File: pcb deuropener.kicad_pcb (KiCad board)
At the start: 2 copper layers, 54.6 x 86.4 mm, 34 parts, among them J1 LED 1, J10 Duo LED, J11 Barrel_Jack_Switch, J12 RFID RC522, J13 Solenoid 12V, J14 jumper, J2 Button 2, J3 LED 2, J4 Button 1, J5 Buzzer 12V, P8 BeagleBone_Black_Header, P9 BeagleBone_Black_Header, Q1 STU60N3LH5, Q2 STU60N3LH5, U1 TSR_1-2450

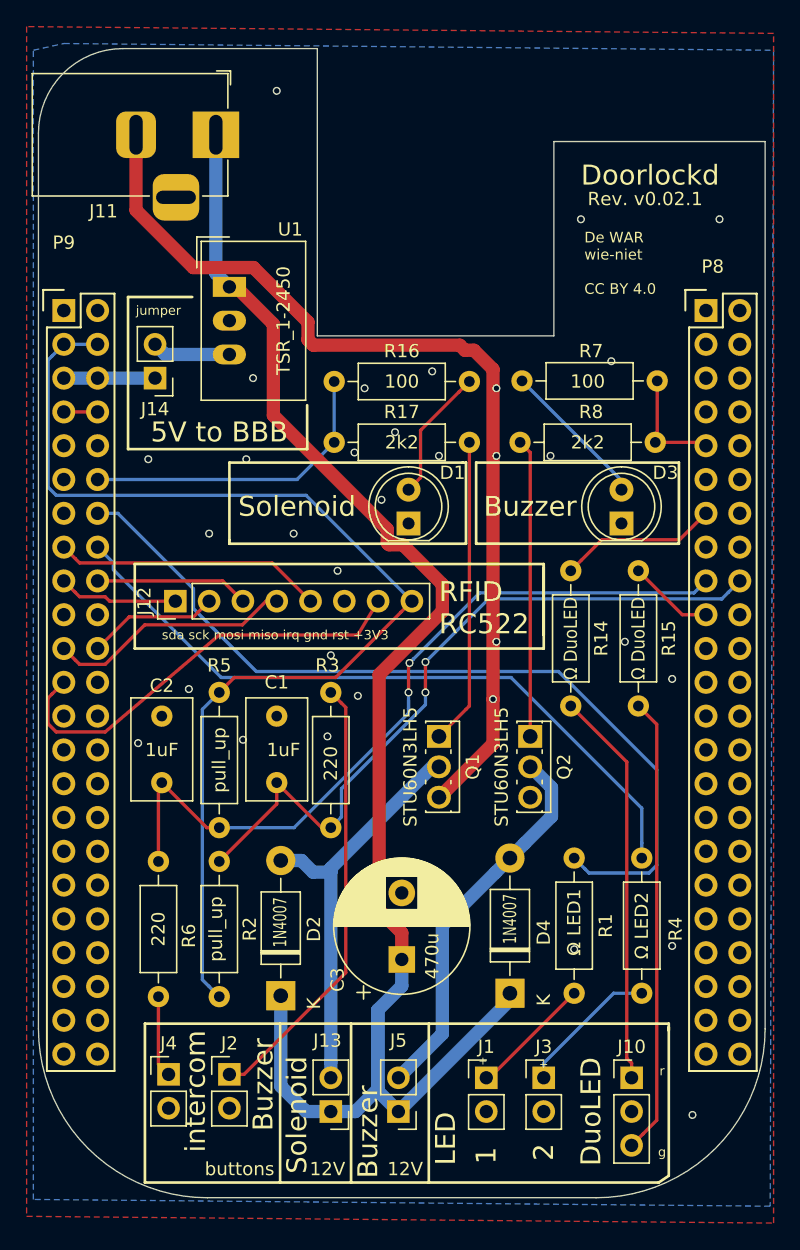
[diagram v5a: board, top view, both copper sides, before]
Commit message: Remove a lot of parts and traces
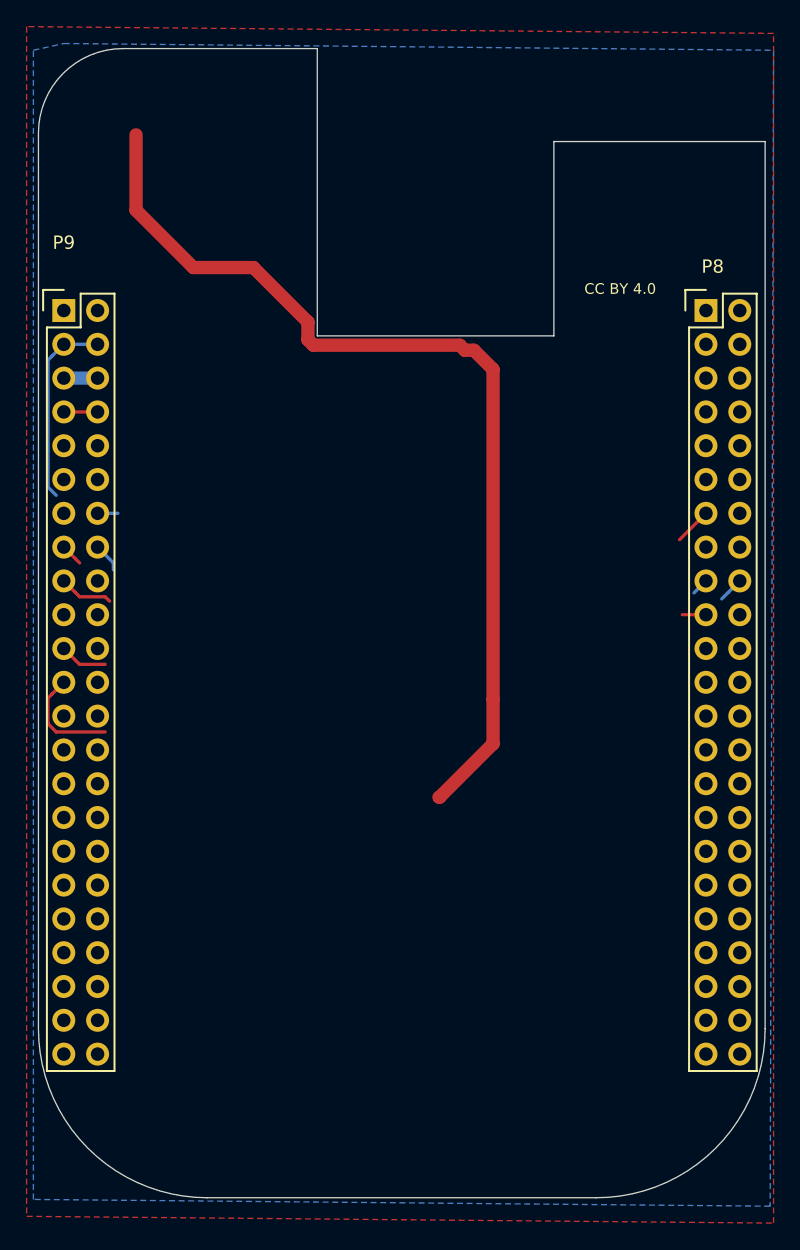
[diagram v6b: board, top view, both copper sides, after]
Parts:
- removed C1, C2: 1uF, Capacitor_THT:C_Disc_D7.5mm_W4.4mm_P5.00mm
- removed C3: 470u, Capacitor_THT:CP_Radial_D10.0mm_P5.00mm
- removed D1, D3: LED, LED_THT:LED_D5.0mm
- removed D2, D4: 1N4007, Diode_THT:D_DO-41_SOD81_P10.16mm_Horizontal
- removed J1: LED 1, Connector_PinHeader_2.54mm:PinHeader_1x02_P2.54mm_Vertical
- removed J10: Duo LED, Connector_PinHeader_2.54mm:PinHeader_1x03_P2.54mm_Vertical
- removed J11: Barrel_Jack_Switch, Connector_BarrelJack:BarrelJack_Horizontal
- removed J12: RFID RC522, Connector_PinHeader_2.54mm:PinHeader_1x08_P2.54mm_Vertical
- removed J13: Solenoid 12V, Connector_PinHeader_2.54mm:PinHeader_1x02_P2.54mm_Vertical
- removed J14: jumper, Connector_PinHeader_2.54mm:PinHeader_1x02_P2.54mm_Vertical
- removed J2: Button 2, Connector_PinHeader_2.54mm:PinHeader_1x02_P2.54mm_Vertical
- removed J3: LED 2, Connector_PinHeader_2.54mm:PinHeader_1x02_P2.54mm_Vertical
- removed J4: Button 1, Connector_PinHeader_2.54mm:PinHeader_1x02_P2.54mm_Vertical
- removed J5: Buzzer 12V, Connector_PinHeader_2.54mm:PinHeader_1x02_P2.54mm_Vertical
- removed Q1, Q2: STU60N3LH5, Package_TO_SOT_THT:SIPAK_Vertical
- removed R1: Ω LED1, Resistor_THT:R_Axial_DIN0207_L6.3mm_D2.5mm_P10.16mm_Horizontal
- removed R14, R15: Ω DuoLED, Resistor_THT:R_Axial_DIN0207_L6.3mm_D2.5mm_P10.16mm_Horizontal
- removed R16, R7: 100, Resistor_THT:R_Axial_DIN0207_L6.3mm_D2.5mm_P10.16mm_Horizontal
- removed R17, R8: 2k2, Resistor_THT:R_Axial_DIN0207_L6.3mm_D2.5mm_P10.16mm_Horizontal
- removed R2, R5: pull_up, Resistor_THT:R_Axial_DIN0207_L6.3mm_D2.5mm_P10.16mm_Horizontal
- removed R3, R6: 220, Resistor_THT:R_Axial_DIN0207_L6.3mm_D2.5mm_P10.16mm_Horizontal
- removed R4: Ω LED2, Resistor_THT:R_Axial_DIN0207_L6.3mm_D2.5mm_P10.16mm_Horizontal
- removed U1: TSR_1-2450, Converter_DCDC:Converter_DCDC_TRACO_TSR-1_THT
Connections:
- P8 pad 10: (no net) -> Net-(P8-Pad10)
- P8 pad 11: (no net) -> Net-(P8-Pad11)
- P8 pad 12: (no net) -> Net-(P8-Pad12)
- P8 pad 13: IO-P8_13-UI_DuoLED1r -> Net-(P8-Pad13)
- P8 pad 14: (no net) -> Net-(P8-Pad14)
- P8 pad 15: (no net) -> Net-(P8-Pad15)
- P8 pad 16: (no net) -> Net-(P8-Pad16)
- P8 pad 17: IO-P8_17-Button1 -> Net-(P8-Pad17)
- P8 pad 18: IO-P8_18-Button2 -> Net-(P8-Pad18)
- P8 pad 19: IO-P8_19-UI_DuoLED1g -> Net-(P8-Pad19)
- P8 pad 20: (no net) -> Net-(P8-Pad20)
- P8 pad 21: (no net) -> Net-(P8-Pad21)
- P8 pad 22: (no net) -> Net-(P8-Pad22)
- P8 pad 23: (no net) -> Net-(P8-Pad23)
- P8 pad 24: (no net) -> Net-(P8-Pad24)
- P8 pad 25: (no net) -> Net-(P8-Pad25)
- P8 pad 26: (no net) -> Net-(P8-Pad26)
- P8 pad 27: (no net) -> Net-(P8-Pad27)
- P8 pad 28: (no net) -> Net-(P8-Pad28)
- P8 pad 29: (no net) -> Net-(P8-Pad29)
- P8 pad 3: (no net) -> Net-(P8-Pad3)
- P8 pad 30: (no net) -> Net-(P8-Pad30)
- P8 pad 31: (no net) -> Net-(P8-Pad31)
- P8 pad 32: (no net) -> Net-(P8-Pad32)
- P8 pad 33: (no net) -> Net-(P8-Pad33)
- P8 pad 34: (no net) -> Net-(P8-Pad34)
- P8 pad 35: (no net) -> Net-(P8-Pad35)
- P8 pad 36: (no net) -> Net-(P8-Pad36)
- P8 pad 37: (no net) -> Net-(P8-Pad37)
- P8 pad 38: (no net) -> Net-(P8-Pad38)
- P8 pad 39: (no net) -> Net-(P8-Pad39)
- P8 pad 4: (no net) -> Net-(P8-Pad4)
- P8 pad 40: (no net) -> Net-(P8-Pad40)
- P8 pad 41: (no net) -> Net-(P8-Pad41)
- P8 pad 42: (no net) -> Net-(P8-Pad42)
- P8 pad 43: (no net) -> Net-(P8-Pad43)
- P8 pad 44: (no net) -> Net-(P8-Pad44)
- P8 pad 45: (no net) -> Net-(P8-Pad45)
- P8 pad 46: (no net) -> Net-(P8-Pad46)
- P8 pad 5: (no net) -> Net-(P8-Pad5)
- P8 pad 6: (no net) -> Net-(P8-Pad6)
- P8 pad 7: (no net) -> Net-(P8-Pad7)
- P8 pad 8: (no net) -> Net-(P8-Pad8)
- P8 pad 9: IO-P8_09-Buzzer -> Net-(P8-Pad9)
- P9 pad 10: (no net) -> Net-(P9-Pad10)
- P9 pad 11: (no net) -> Net-(P9-Pad11)
- P9 pad 12: IO-P9_12-Solenoid -> Net-(P9-Pad12)
- P9 pad 13: (no net) -> Net-(P9-Pad13)
- P9 pad 14: IO-P9_14-UILED1 -> Net-(P9-Pad14)
- P9 pad 15: IO-P9_15-RC522_IRQ -> Net-(P9-Pad15)
- P9 pad 16: IO-P9_16-UILED2 -> Net-(P9-Pad16)
- P9 pad 17: IO-P9_17-RC522_SDA -> Net-(P9-Pad17)
- P9 pad 18: IO-P9_18-RC522_MOSI -> Net-(P9-Pad18)
- P9 pad 19: (no net) -> Net-(P9-Pad19)
- P9 pad 20: (no net) -> Net-(P9-Pad20)
- P9 pad 21: IO-P9_21-RC522_MISO -> Net-(P9-Pad21)
- P9 pad 22: IO-P9_22-RC522_SCK -> Net-(P9-Pad22)
- P9 pad 23: IO-P9_23-RC522_RST -> Net-(P9-Pad23)
- P9 pad 24: (no net) -> Net-(P9-Pad24)
- P9 pad 25: (no net) -> Net-(P9-Pad25)
- P9 pad 26: (no net) -> Net-(P9-Pad26)
- P9 pad 27: (no net) -> Net-(P9-Pad27)
- P9 pad 28: (no net) -> Net-(P9-Pad28)
- P9 pad 29: (no net) -> Net-(P9-Pad29)
- P9 pad 30: (no net) -> Net-(P9-Pad30)
- P9 pad 31: (no net) -> Net-(P9-Pad31)
- P9 pad 32: (no net) -> VDD_ADC
- P9 pad 33: (no net) -> Net-(P9-Pad33)
- P9 pad 34: (no net) -> GNDA_ADC
- P9 pad 35: (no net) -> Net-(P9-Pad35)
- P9 pad 36: (no net) -> Net-(P9-Pad36)
- P9 pad 37: (no net) -> Net-(P9-Pad37)
- P9 pad 38: (no net) -> Net-(P9-Pad38)
- P9 pad 39: (no net) -> Net-(P9-Pad39)
- P9 pad 40: (no net) -> Net-(P9-Pad40)
- P9 pad 41: (no net) -> Net-(P9-Pad41)
- P9 pad 42: (no net) -> Net-(P9-Pad42)
- P9 pad 9: (no net) -> Net-(P9-Pad9)
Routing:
- net +12V: track 119.3 -> 0.00 mm
- net +3V3: track 85.9 -> 14.6 mm
- net IO-P9_14-UILED1: track 65.0 -> 0.00 mm
- net IO-P8_17-Button1: track 58.8 -> 0.00 mm, vias 2 -> 0
- net IO-P8_18-Button2: track 54.7 -> 0.00 mm, vias 2 -> 0
- net IO-P9_16-UILED2: track 53.1 -> 0.00 mm
- net Net-(J10-Pad3): track 34.4 -> 0.00 mm
- net Net-(J2-Pad1): track 33.4 -> 0.00 mm
- net IO-P9_23-RC522_RST: track 32.8 -> 0.00 mm
- net Net-(D2-Pad2): track 31.3 -> 0.00 mm
- net Net-(J10-Pad1): track 29.8 -> 0.00 mm
- net Net-(D4-Pad2): track 28.8 -> 0.00 mm
- net IO-P9_12-Solenoid: track 23.5 -> 0.00 mm
- net Net-(Q1-Pad1): track 23.0 -> 0.00 mm
- net Net-(Q2-Pad1): track 22.4 -> 0.00 mm
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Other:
- board text added: "CC BY 4.0"
- board text removed: "+"
- board text removed: "1"
- board text removed: "12V"
- board text removed: "2"
- board text removed: "5V to BBB"
- board text removed: "Buzzer"
- board text removed: "De WAR wie-niet CC BY 4.0"
- board text removed: "Doorlockd"
- board text removed: "DuoLED"
- board text removed: "LED"
- board text removed: "RFID RC522"
- board text removed: "Rev. v0.02.1"
- board text removed: "Solenoid"
- board text removed: "buttons"
- board text removed: "g"
- board text removed: "intercom"
- board text removed: "jumper"
- board text removed: "r"
- board text removed: "sda sck mosi miso irq gnd rst +3V3"

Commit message: convert to kicad 6
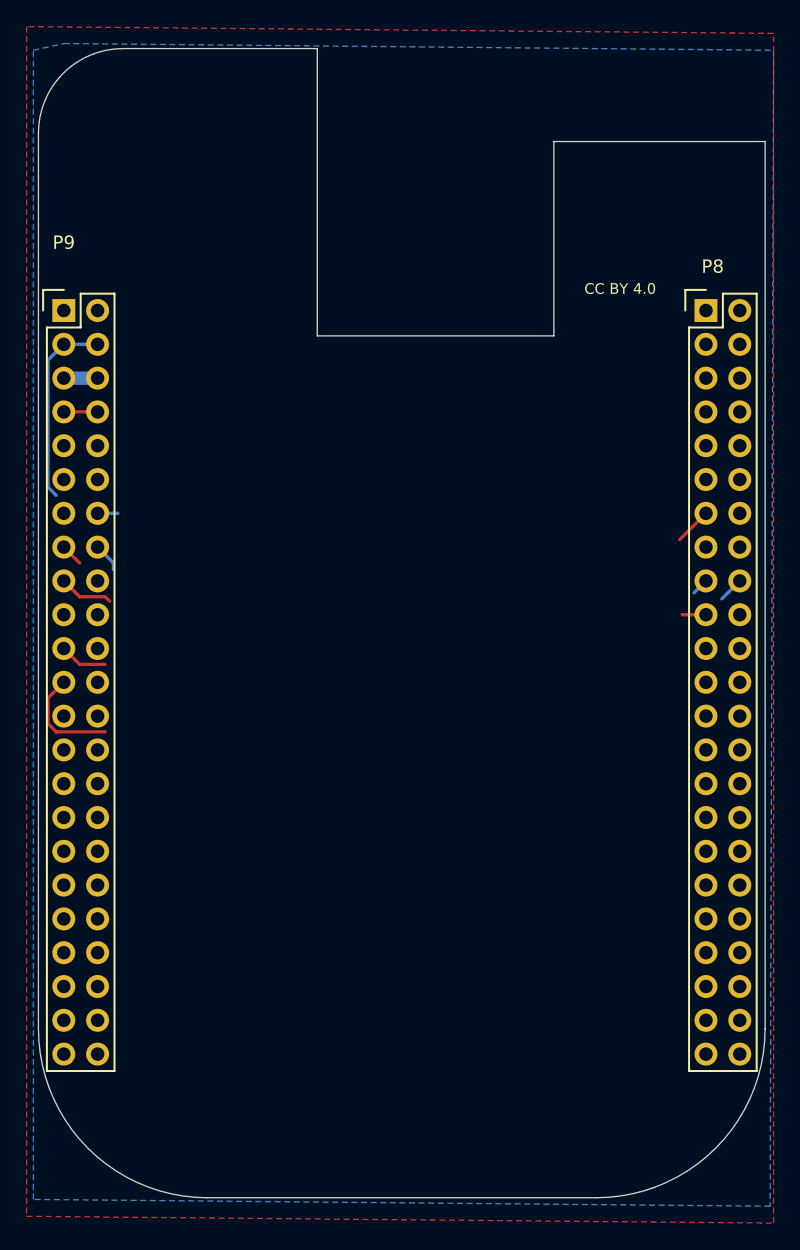
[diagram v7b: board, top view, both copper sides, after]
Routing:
- net Earth: track 72.1 -> 0.00 mm
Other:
- outline, holes or cut-outs redrawn
- net class Default removed
- net class thicker removed
